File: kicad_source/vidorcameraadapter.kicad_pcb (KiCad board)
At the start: 2 copper layers, 62 x 63 mm, 62 parts, among them CN1 CONN_02X26, CN2 CONN_02X10, CN3 CONN_01X03

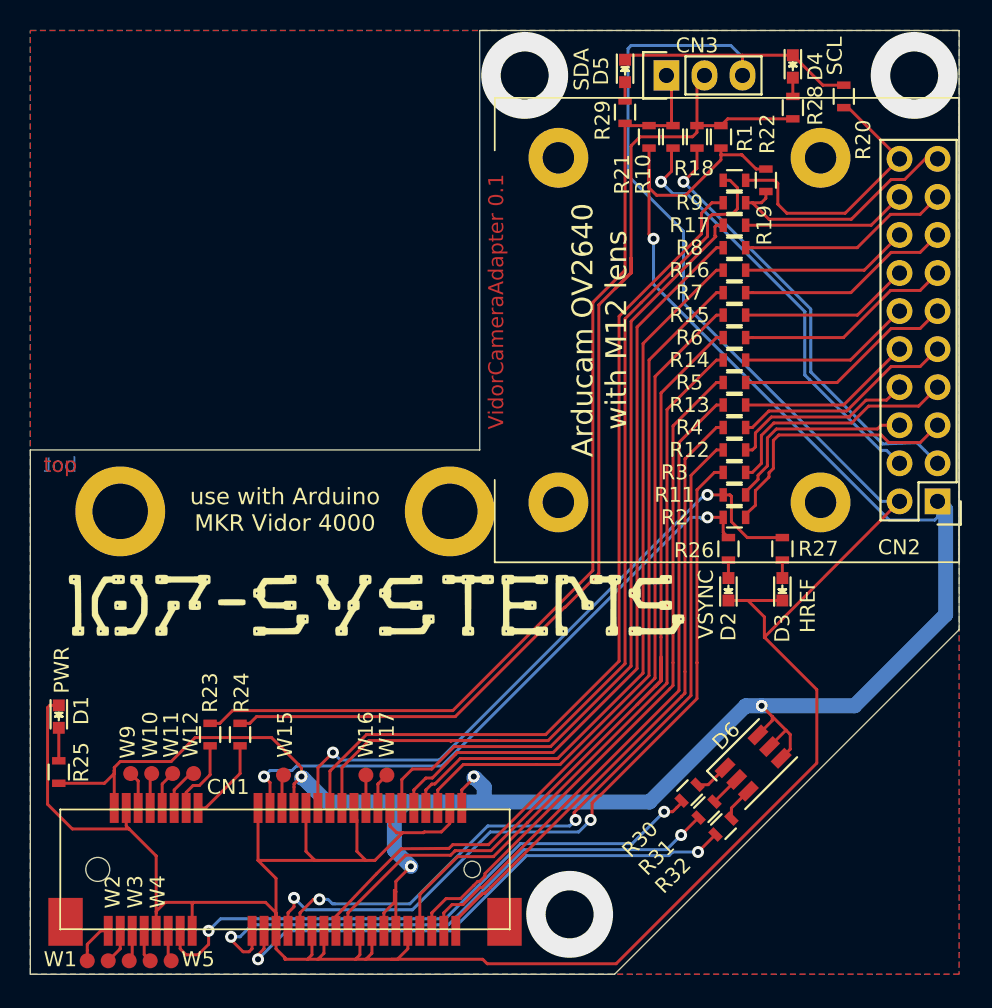
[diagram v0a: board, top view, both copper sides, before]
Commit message: added jumper for I2C pullup, added buffer ic for I2C leds, made mounting holes as parts, made DRC, updated images
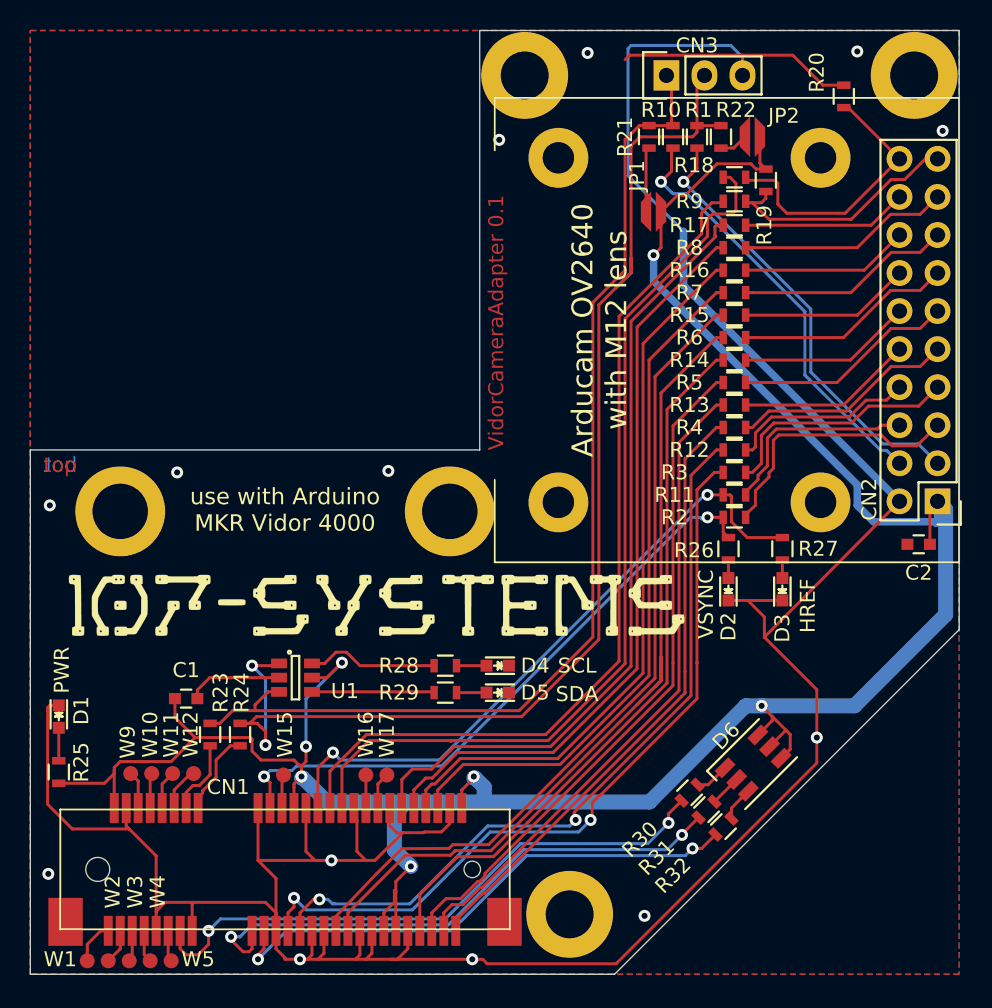
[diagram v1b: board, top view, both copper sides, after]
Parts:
- added C1: 100nF, capacitors:C_0603, F.Cu at (88.4, 118.6)
- added C2: 100nF, capacitors:C_0603, F.Cu at (137.3, 108.3)
- added JP1: Jumper_NC_Small, wire_pads:SolderJumper_2mm, F.Cu at (119.6, 86.1)
- added JP2: Jumper_NC_Small, wire_pads:SolderJumper_2mm, F.Cu at (126.2, 81.1)
- added MECH7: MHP_3.2_5.8, MECH_mounting_holes:MHP_3.2_5.8, F.Cu at (114.0, 133.0)
- added MECH8: MHP_3.2_5.8, MECH_mounting_holes:MHP_3.2_5.8, F.Cu at (111.0, 77.0)
- added MECH9: MHP_3.2_5.8, MECH_mounting_holes:MHP_3.2_5.8, F.Cu at (137.0, 77.0)
- added U1: SN74LVC2G34DBV, SOT_TO:SOT-23-6, F.Cu at (95.7, 117.2)
- CN1: value CONN_02X26 -> TE_2041119-2
- CN2: value CONN_02X10 -> RS2-20-G
- CN3: value CONN_01X03 -> DNI
- D1: value Led_Small -> Led yellow
- D2, D4: value Led_Small -> Led green
- D3, D5: value Led_Small -> Led red
- D6: value LED_RGB -> 150353M153300
- moved D4 44.6 mm to (109.2, 116.4), turned to 180 degrees
- moved R28 43.9 mm to (105.7, 116.4), turned to 180 degrees
- moved D5 42.4 mm to (109.2, 118.2), turned to 180 degrees
- moved R29 40.6 mm to (105.7, 118.2), turned to 180 degrees
- moved R18 0.20 mm to (125.0, 83.8)
- moved R9 0.10 mm to (125.0, 85.4)
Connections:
- R21 pad 1: +3V3 -> Net-(JP1-Pad2)
- R22 pad 1: +3V3 -> Net-(JP2-Pad2)
- R28 pad 2: /SCL -> /SCL_B
- R29 pad 2: /SDA -> /SDA_B
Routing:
- net +3V3: track 152.8 -> 166.3 mm, vias 5 -> 7
- net /SCL_B: track 0.00 -> 8.83 mm
- net /SDA_B: track 0.00 -> 8.17 mm
- net /SCL: track 74.7 -> 82.6 mm, vias 0 -> 2
- net GND: track 216.2 -> 221.8 mm, vias 0 -> 13
- net Net-(JP1-Pad2): track 0.00 -> 4.33 mm
- net /SDA: track 67.3 -> 71.4 mm
- net Net-(JP2-Pad2): track 0.00 -> 1.91 mm
- net Net-(D5-Pad2): track 1.25 -> 2.00 mm
- net Net-(D4-Pad2): track 1.25 -> 2.00 mm
- net (no net): vias 3 -> 0

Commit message: moved pins on the Vidor connector to free NINA pins and pins with pull up, exchanged PCLK and XCLK, added pdfs and generated images
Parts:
- moved W10 14.0 mm to (92.4, 136.1)
- moved W11 10.1 mm to (97.6, 123.7)
- moved W12 10.1 mm to (99.0, 123.7)
- moved W5 6.40 mm to (93.8, 136.1)
- moved C1 3.74 mm to (91.5, 116.5), turned to 270 degrees
- moved R23 2.46 mm to (91.1, 118.8), turned to 180 degrees
- moved R24 1.03 mm to (91.1, 120.5), turned to 180 degrees
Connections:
- CN1 pad 10: /RSVD6 -> /SDA_V
- CN1 pad 11: /RSVD7 -> /LED_G
- CN1 pad 12: /RSVD8 -> /SCL_V
- CN1 pad 13: /LED_R -> /LED_B
- CN1 pad 14: /SDA_V -> /RST
- CN1 pad 16: /SCL_V -> /PWDN
- CN1 pad 17: /LED_G -> /RSVD5
- CN1 pad 19: /LED_B -> /RSVD7
- CN1 pad 23: /PCLK -> /XCLK
- CN1 pad 25: /XCLK -> /PCLK
- CN1 pad 30: /RST -> /RSVD6
- CN1 pad 32: /PWDN -> /RSVD8
- CN1 pad 8: /RSVD5 -> /LED_R
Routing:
- net GND: track 221.8 -> 231.6 mm, vias 13 -> 15
- net /RST: track 58.7 -> 67.8 mm
- net /PWDN: track 64.4 -> 73.5 mm
- net /LED_B: track 36.1 -> 41.5 mm
- net /LED_R: track 40.0 -> 44.5 mm
- net /LED_G: track 37.7 -> 42.1 mm
- net +3V3: track 166.3 -> 170.5 mm, vias 7 -> 6
- net /SDA_V: track 5.06 -> 8.83 mm
- net /SDA: track 71.4 -> 69.5 mm
- net /PCLK: track 52.2 -> 50.6 mm
- net /SCL: track 82.6 -> 81.2 mm
- net /XCLK: track 51.5 -> 52.9 mm
- net /RSVD7: track 2.08 -> 3.28 mm
- net /SCL_V: track 5.69 -> 6.77 mm
- net /RSVD5: track 2.34 -> 3.37 mm
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
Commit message: changed pinning to fit to https://github.com/107-systems/viper-vidor-fpga
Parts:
- moved W9 12.8 mm to (87.4, 136.1)
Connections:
- CN1 pad 11: /LED_G -> /RSVD3
- CN1 pad 13: /LED_B -> /DOUT6
- CN1 pad 23: /XCLK -> /PCLK
- CN1 pad 25: /PCLK -> /DOUT4
- CN1 pad 31: /DOUT4 -> /DOUT5
- CN1 pad 33: /DOUT5 -> /DOUT7
- CN1 pad 45: /DOUT6 -> /LED_B
- CN1 pad 47: /DOUT7 -> /XCLK
- CN1 pad 6: /RSVD3 -> /LED_G
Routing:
- net /LED_B: track 41.5 -> 25.8 mm
- net /DOUT6: track 48.1 -> 63.8 mm, vias 0 -> 2
- net /XCLK: track 52.9 -> 43.4 mm
- net /DOUT7: track 45.6 -> 51.4 mm
- net GND: track 231.6 -> 236.9 mm, vias 15 -> 19
- net /LED_G: track 42.1 -> 46.0 mm
- net /DOUT4: track 55.3 -> 58.0 mm
- net /PCLK: track 50.6 -> 53.0 mm
- net /DOUT5: track 58.4 -> 60.4 mm
- net +3V3: track 170.5 -> 168.7 mm
